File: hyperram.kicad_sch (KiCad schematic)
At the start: 7 parts, among them U11 S27KL0641DABHI023

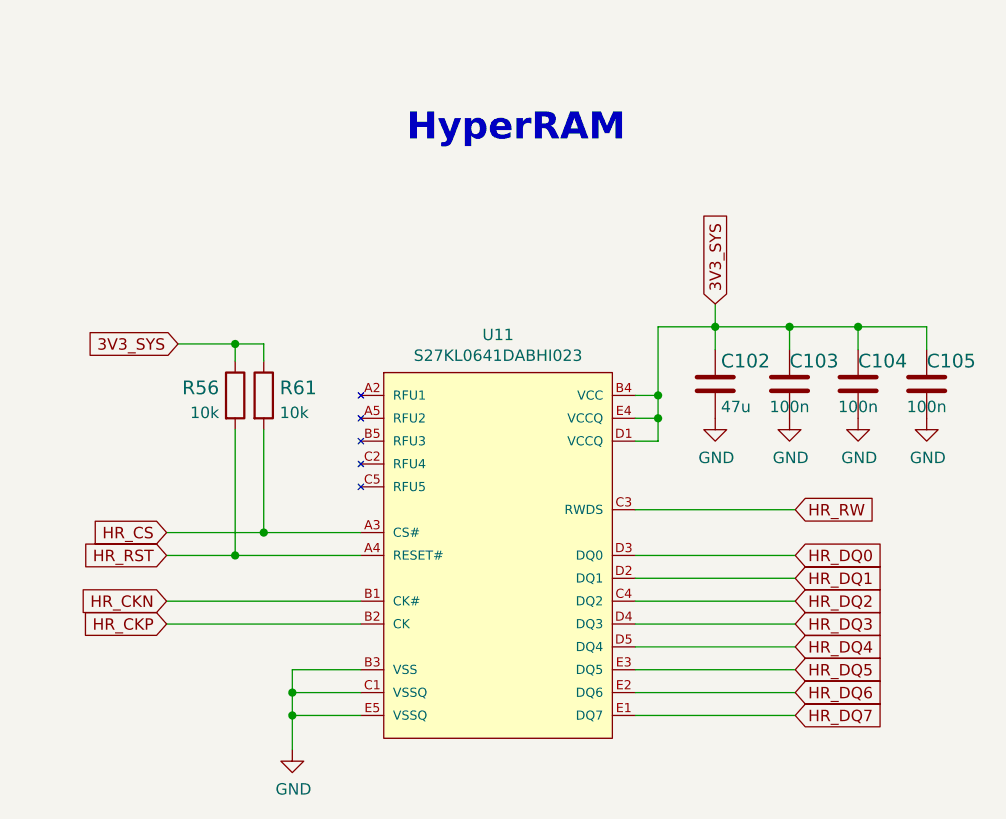
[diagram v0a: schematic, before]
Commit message: Rebase to Rev. 1.2.2
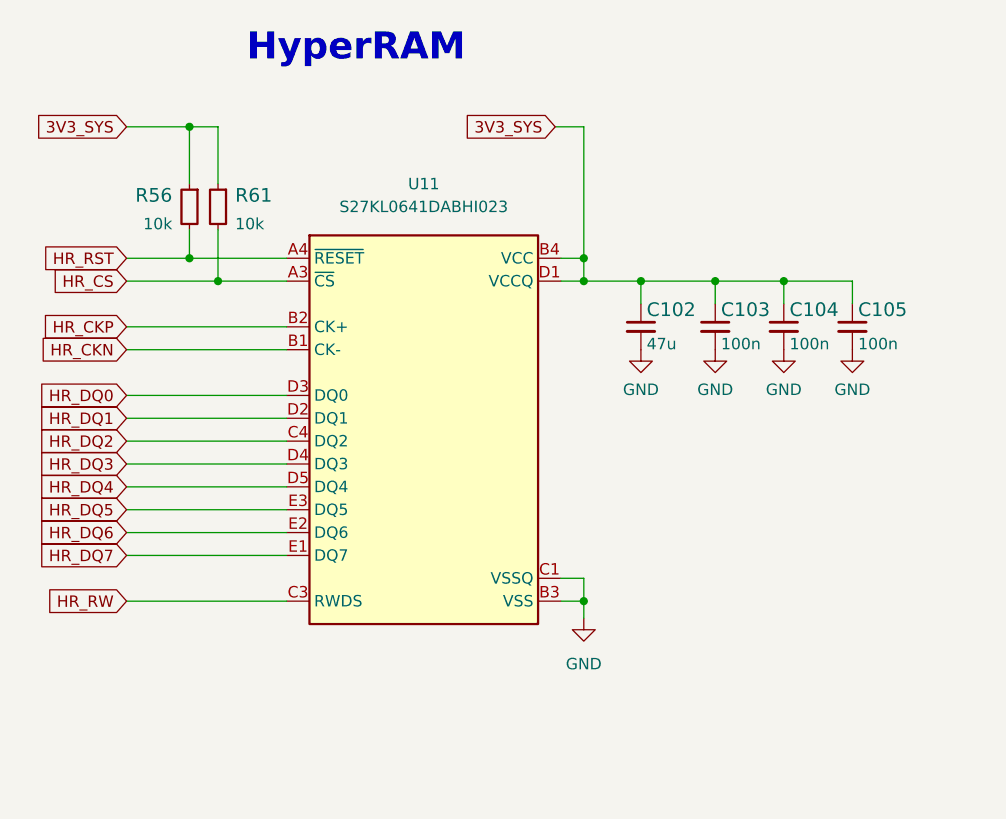
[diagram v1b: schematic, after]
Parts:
- removed C102: C_47u_0603, data-center-dram-tester-footprints:0603-cap, symbol data-center-dram-tester:C_47u_0603
- removed C103, C104, C105: C_100n_0402, antmicro-footprints:0402-cap, symbol antmicroCapacitors0402:C_100n_0402
- removed R56, R61: R_10k_0402, data-center-dram-tester-footprints:0402-res, symbol data-center-dram-tester:R_10k_0402
- removed U11: S27KL0641DABHI023, data-center-dram-tester-footprints:FBGA-24, symbol data-center-dram-tester:S27KL0641DABHI023
- added C102: C_47u_0603, data-center-rdimm-ddr4-tester-footprints:C_0603_1608Metric, symbol data-center-rdimm-ddr4-tester:C_47u_0603
- added C103, C104, C105: C_100n_0402, data-center-rdimm-ddr4-tester-footprints:C_0402_1005Metric, symbol data-center-rdimm-ddr4-tester:C_100n_0402
- added R56, R61: R_10k_0402, data-center-rdimm-ddr4-tester-footprints:R_0402_1005Metric, symbol data-center-rdimm-ddr4-tester:R_10k_0402
- added U11: S27KL0641DABHI023, data-center-rdimm-ddr4-tester-footprints:FBGA-24-1_6x8mm_Layout5x5_P1mm, symbol data-center-rdimm-ddr4-tester:S27KL0641DABHI023
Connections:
- net 3V3_SYS: now also C102.1, C103.1, C104.1, C105.1, R56.1, R61.1, U11.B4 (VCC), U11.D1 (VCCQ), U11.E4 (VCCQ)
- net GND: now also C102.2, C103.2, C104.2, C105.2, U11.B3 (VSS), U11.C1 (VSSQ), U11.E5 (VSSQ)
- net HR_CKN: now also U11.B1 (CK-)
- net HR_CKP: now also U11.B2 (CK+)
- net HR_CS: now also R61.2, U11.A3 (~{CS})
- net HR_DQ0: now also U11.D3 (DQ0)
- net HR_DQ1: now also U11.D2 (DQ1)
- net HR_DQ2: now also U11.C4 (DQ2)
- net HR_DQ3: now also U11.D4 (DQ3)
- net HR_DQ4: now also U11.D5 (DQ4)
- net HR_DQ5: now also U11.E3 (DQ5)
- net HR_DQ6: now also U11.E2 (DQ6)
- net HR_DQ7: now also U11.E1 (DQ7)
- net HR_RST: now also R56.2, U11.A4 (~{RESET})
- net HR_RW: now also U11.C3 (RWDS)
- new net: U11.A2 (NC), U11.A5 (NC), U11.B5 (NC), U11.C2 (NC), U11.C5 (NC)

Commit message: Update designators and sync schematic with PCB
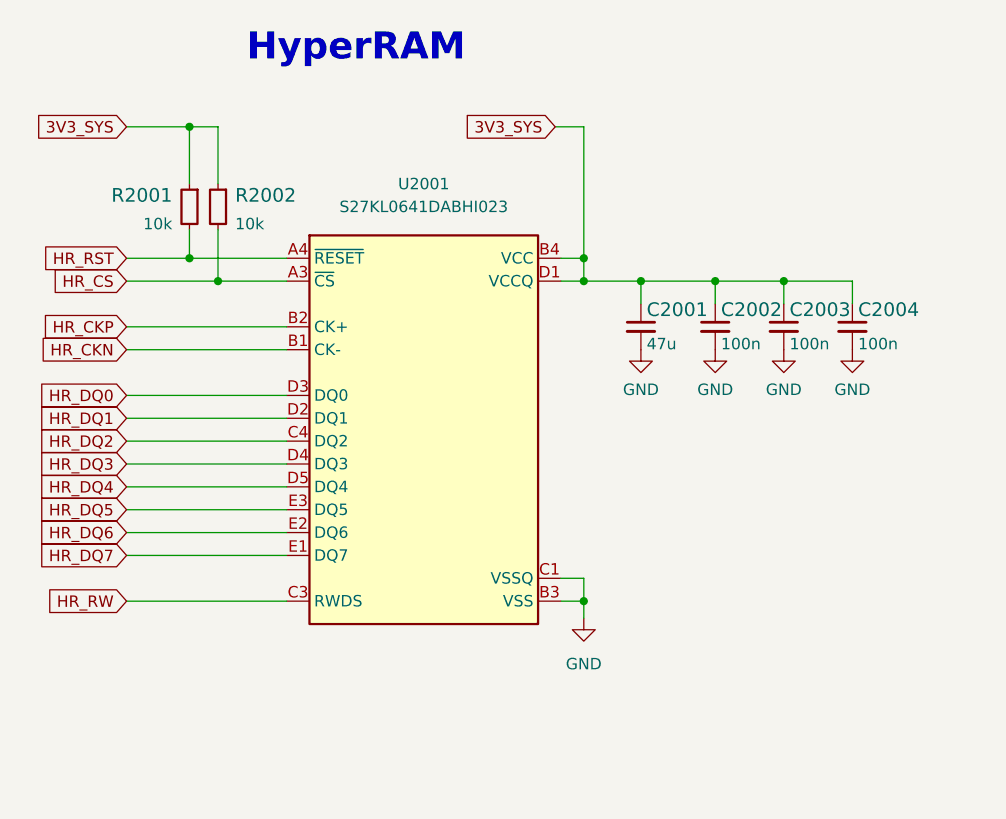
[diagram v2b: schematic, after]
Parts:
- renumbered C102 to C2001, C103 to C2002, C104 to C2003, C105 to C2004, R56 to R2001, R61 to R2002, U11 to U2001
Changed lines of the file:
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@@
   (symbol (lib_id "data-center-rdimm-ddr4-tester:S27KL0641DABHI023") (at 190.5 126.365 0) (unit 1)
     (in_bom yes) (on_board yes) (fields_autoplaced)
-    (property "Reference" "U11" (id 0) (at 205.74 118.11 0))
+    (property "Reference" "U2001" (id 0) (at 205.74 118.11 0))
     (property "Value" "S27KL0641DABHI023" (id 1) (at 205.74 172.72 0)
       (effects (font (size 1.27 1.27) (thickness 0.15)) hide)
@@
   (symbol (lib_id "data-center-rdimm-ddr4-tester:C_47u_0603") (at 229.87 131.445 270) (unit 1)
     (in_bom yes) (on_board yes)
-    (property "Reference" "C102" (id 0) (at 230.505 132.08 90)
+    (property "Reference" "C2001" (id 0) (at 230.505 132.08 90)
       (effects (font (size 1.524 1.524)) (justify left))
     )
@@
   (symbol (lib_id "data-center-rdimm-ddr4-tester:C_100n_0402") (at 245.745 131.445 270) (unit 1)
     (in_bom yes) (on_board yes)
-    (property "Reference" "C104" (id 0) (at 246.38 132.08 90)
+    (property "Reference" "C2003" (id 0) (at 246.38 132.08 90)
       (effects (font (size 1.524 1.524)) (justify left))
     )
@@
   (symbol (lib_id "data-center-rdimm-ddr4-tester:GND") (at 229.87 136.525 0) (unit 1)
     (in_bom yes) (on_board yes) (fields_autoplaced)
-    (property "Reference" "#PWR0260" (id 0) (at 229.87 142.875 0)
+    (property "Reference" "#PWR02002" (id 0) (at 229.87 142.875 0)
       (effects (font (size 1.27 1.27)) hide)
     )
@@
   (symbol (lib_id "data-center-rdimm-ddr4-tester:R_10k_0402") (at 179.705 118.11 270) (unit 1)
     (in_bom yes) (on_board yes)
-    (property "Reference" "R56" (id 0) (at 177.8 119.3801 90)
+    (property "Reference" "R2001" (id 0) (at 177.8 119.3801 90)
       (effects (font (size 1.524 1.524)) (justify right))
     )
@@
   (symbol (lib_id "data-center-rdimm-ddr4-tester:GND") (at 238.125 136.525 0) (unit 1)
     (in_bom yes) (on_board yes) (fields_autoplaced)
-    (property "Reference" "#PWR0261" (id 0) (at 238.125 142.875 0)
+    (property "Reference" "#PWR02003" (id 0) (at 238.125 142.875 0)
       (effects (font (size 1.27 1.27)) hide)
     )
@@
   (symbol (lib_id "data-center-rdimm-ddr4-tester:GND") (at 245.745 136.525 0) (unit 1)
     (in_bom yes) (on_board yes) (fields_autoplaced)
-    (property "Reference" "#PWR0262" (id 0) (at 245.745 142.875 0)
+    (property "Reference" "#PWR02004" (id 0) (at 245.745 142.875 0)
       (effects (font (size 1.27 1.27)) hide)
     )
@@
   (symbol (lib_id "data-center-rdimm-ddr4-tester:C_100n_0402") (at 238.125 131.445 270) (unit 1)
     (in_bom yes) (on_board yes)
-    (property "Reference" "C103" (id 0) (at 238.76 132.08 90)
+    (property "Reference" "C2002" (id 0) (at 238.76 132.08 90)
       (effects (font (size 1.524 1.524)) (justify left))
     )
@@
   (symbol (lib_id "data-center-rdimm-ddr4-tester:R_10k_0402") (at 182.88 118.11 270) (unit 1)
     (in_bom yes) (on_board yes) (fields_autoplaced)
-    (property "Reference" "R61" (id 0) (at 184.785 119.38 90)
+    (property "Reference" "R2002" (id 0) (at 184.785 119.38 90)
       (effects (font (size 1.524 1.524)) (justify left))
     )
@@
   (symbol (lib_id "data-center-rdimm-ddr4-tester:GND") (at 223.52 166.37 0) (unit 1)
     (in_bom yes) (on_board yes) (fields_autoplaced)
-    (property "Reference" "#PWR0263" (id 0) (at 223.52 172.72 0)
+    (property "Reference" "#PWR02001" (id 0) (at 223.52 172.72 0)
       (effects (font (size 1.27 1.27)) hide)
     )
@@
   (symbol (lib_id "data-center-rdimm-ddr4-tester:C_100n_0402") (at 253.365 131.445 270) (unit 1)
     (in_bom yes) (on_board yes)
-    (property "Reference" "C105" (id 0) (at 254 132.08 90)
+    (property "Reference" "C2004" (id 0) (at 254 132.08 90)
       (effects (font (size 1.524 1.524)) (justify left))
     )
@@
   (symbol (lib_id "data-center-rdimm-ddr4-tester:GND") (at 253.365 136.525 0) (unit 1)
     (in_bom yes) (on_board yes) (fields_autoplaced)
-    (property "Reference" "#PWR0264" (id 0) (at 253.365 142.875 0)
-      (effects (font (size 1.27 1.27)) hide)
-    )
+    (property "Reference" "#PWR02005" (id 0) (at 253.365 142.875 0)
+      (effects (font (size 1.27 1.27)) hide)
+    )

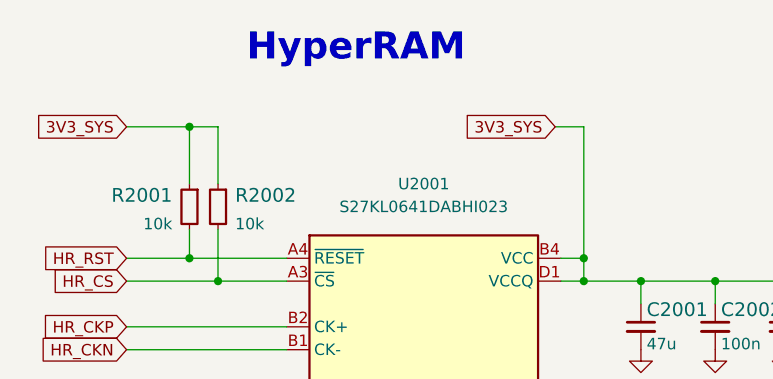
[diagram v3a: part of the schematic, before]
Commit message: Replace supply labels with proper symbols
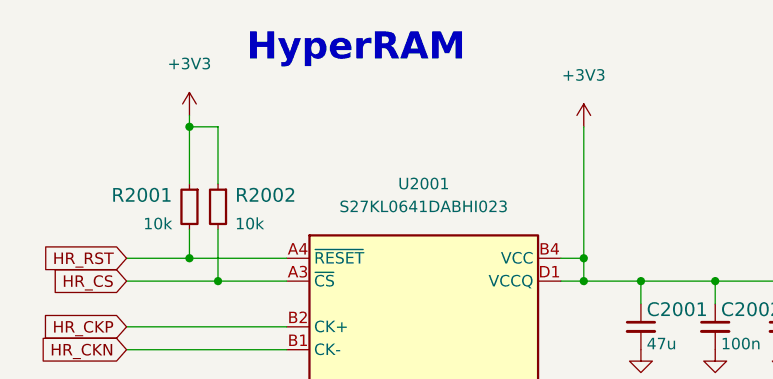
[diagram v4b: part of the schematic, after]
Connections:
- net 3V3_SYS renamed +3V3
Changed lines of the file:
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@@
+    (stroke (width 0) (type default) (color 0 0 0 0))
+  )
+  (wire (pts (xy 179.705 110.49) (xy 179.705 111.76))
     (stroke (width 0) (type default) (color 0 0 0 0))
   )
@@
   )
   (wire (pts (xy 223.52 164.465) (xy 223.52 166.37))
-    (stroke (width 0) (type default) (color 0 0 0 0))
-  )
-  (wire (pts (xy 223.52 111.76) (xy 220.345 111.76))
-    (stroke (width 0) (type default) (color 0 0 0 0))
-  )
-  (wire (pts (xy 179.705 111.76) (xy 172.72 111.76))
     (stroke (width 0) (type default) (color 0 0 0 0))
   )
@@
     )
   )
-  (global_label "3V3_SYS" (shape input) (at 220.345 111.76 180) (fields_autoplaced)
-    (effects (font (size 1.27 1.27)) (justify right))
-    (property "Intersheet References" "${INTERSHEET_REFS}" (id 0) (at 210.0379 111.8394 0)
-      (effects (font (size 1.27 1.27)) (justify right) hide)
-    )
-  )
   (global_label "HR_CKN" (shape input) (at 172.72 136.525 180) (fields_autoplaced)
     (effects (font (size 1.27 1.27)) (justify right))
@@
     (effects (font (size 1.27 1.27)) (justify right))
     (property "Intersheet References" "${INTERSHEET_REFS}" (id 0) (at 163.0177 159.3056 0)
-      (effects (font (size 1.27 1.27)) (justify right) hide)
-    )
-  )
-  (global_label "3V3_SYS" (shape input) (at 172.72 111.76 180) (fields_autoplaced)
-    (effects (font (size 1.27 1.27)) (justify right))
-    (property "Intersheet References" "${INTERSHEET_REFS}" (id 0) (at 162.4129 111.6806 0)
       (effects (font (size 1.27 1.27)) (justify right) hide)
     )
@@
     )
     (pin "1")
+  )
+  (symbol (lib_id "power:+3V3") (at 179.705 110.49 0) (unit 1)
+    (in_bom yes) (on_board yes) (fields_autoplaced)
+    (property "Reference" "#PWR?" (id 0) (at 179.705 114.3 0)
+      (effects (font (size 1.27 1.27)) hide)
+    )
+    (property "Value" "+3V3" (id 1) (at 179.705 104.775 0))
+    (property "Footprint" "" (id 2) (at 179.705 110.49 0)
+      (effects (font (size 1.27 1.27)) hide)
+    )
+    (property "Datasheet" "" (id 3) (at 179.705 110.49 0)
+      (effects (font (size 1.27 1.27)) hide)
+    )
+    (pin "1")
+  )
+  (symbol (lib_id "power:+3V3") (at 223.52 111.76 0) (unit 1)
+    (in_bom yes) (on_board yes) (fields_autoplaced)
+    (property "Reference" "#PWR?" (id 0) (at 223.52 115.57 0)
+      (effects (font (size 1.27 1.27)) hide)
+    )
+    (property "Value" "+3V3" (id 1) (at 223.52 106.045 0))
+    (property "Footprint" "" (id 2) (at 223.52 111.76 0)
+      (effects (font (size 1.27 1.27)) hide)
+    )
+    (property "Datasheet" "" (id 3) (at 223.52 111.76 0)
+      (effects (font (size 1.27 1.27)) hide)
+    )
+    (pin "1")

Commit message: Add loclib
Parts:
- C2001: footprint data-center-rdimm-ddr4-tester-footprints:C_0603_1608Metric -> sodimm-ddr5-tester-footprints:C_0603_1608Metric; symbol data-center-rdimm-ddr4-tester:C_47u_0603 -> sodimm-ddr5-tester:C_47u_0603
- C2002, C2003, C2004: footprint data-center-rdimm-ddr4-tester-footprints:C_0402_1005Metric -> sodimm-ddr5-tester-footprints:C_0402_1005Metric; symbol data-center-rdimm-ddr4-tester:C_100n_0402 -> sodimm-ddr5-tester:C_100n_0402
- R2001, R2002: footprint data-center-rdimm-ddr4-tester-footprints:R_0402_1005Metric -> sodimm-ddr5-tester-footprints:R_0402_1005Metric; symbol data-center-rdimm-ddr4-tester:R_10k_0402 -> sodimm-ddr5-tester:R_10k_0402
- U2001: footprint data-center-rdimm-ddr4-tester-footprints:FBGA-24-1_6x8mm_Layout5x5_P1mm -> sodimm-ddr5-tester-footprints:FBGA-24-1_6x8mm_Layout5x5_P1mm; symbol data-center-rdimm-ddr4-tester:S27KL0641DABHI023 -> sodimm-ddr5-tester:S27KL0641DABHI023
